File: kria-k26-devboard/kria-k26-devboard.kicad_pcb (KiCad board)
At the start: 8 copper layers, 121.5 x 89.8 mm, 225 parts, among them IC1 TPS2378DDA, IC2 USB5534B-5000JZX, J1 5-2337992-8, J2 USB4105-GF-A, J3 DC_SOCKET, J6 685119134923_, J7 WE_68715014022, M1 XILINX-KRIA-K26, P1 2199119-6, Q1 PJA3441, Q2 BSS138DW-7-F, U1 FT4232HPQ, U10 AP62301WU-7, U11 AP62301WU-7, U12 LTC4358CDE, U13 LTC4358CDE, U14 LTC4358CDE, U15 DP83867CRRGZR, U16 USB3310C-CP, U17 TPD4E05U06QDQARQ1, U18 TPD4E05U06QDQARQ1, U19 GSB3112311HR, U2 AP62301WU-7, U20 TPD4E05U06QDQARQ1, U21 TPD4E05U06QDQARQ1, U22 GSB3112311HR, U23 NVT4858HKZ, U3 MAX5984AETI+T, U4 AP62301WU-7, U5 AP62301WU-7, U6 AP62301WU-7, U7 AP62301WU-7, U8 RPX-4.0-R, U9 AP62301WU-7, Y1 ABM8G-25.000MHZ-18-D2Y-T

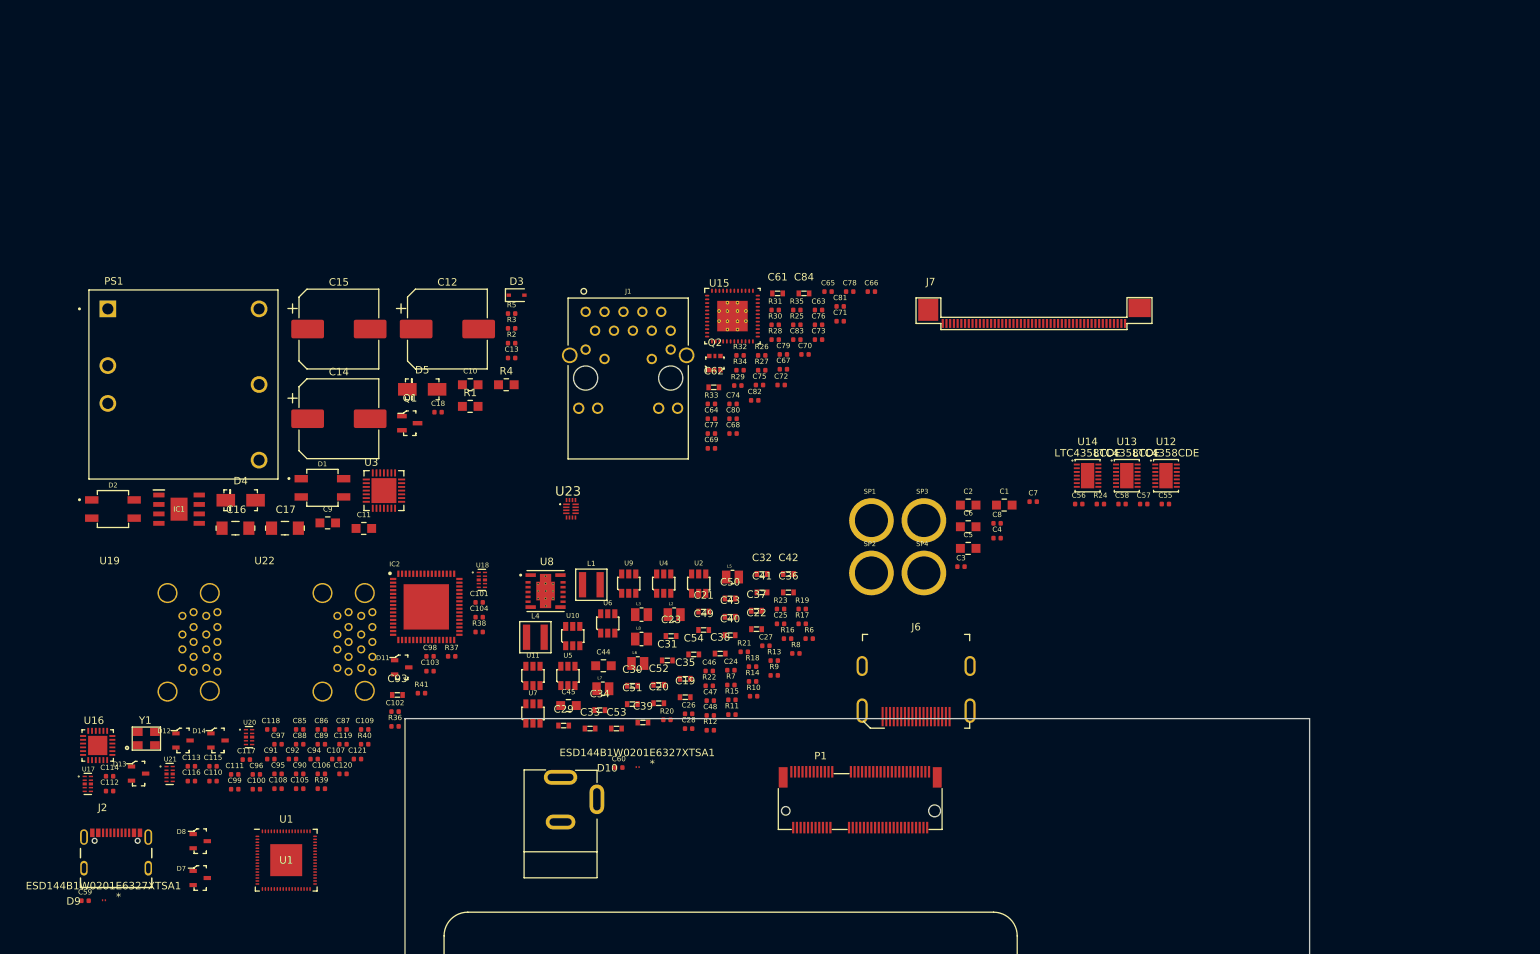
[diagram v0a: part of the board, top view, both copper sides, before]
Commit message: Finished reset logic, added crystal gen. to USB PHY, create power toggle for SD 3.0
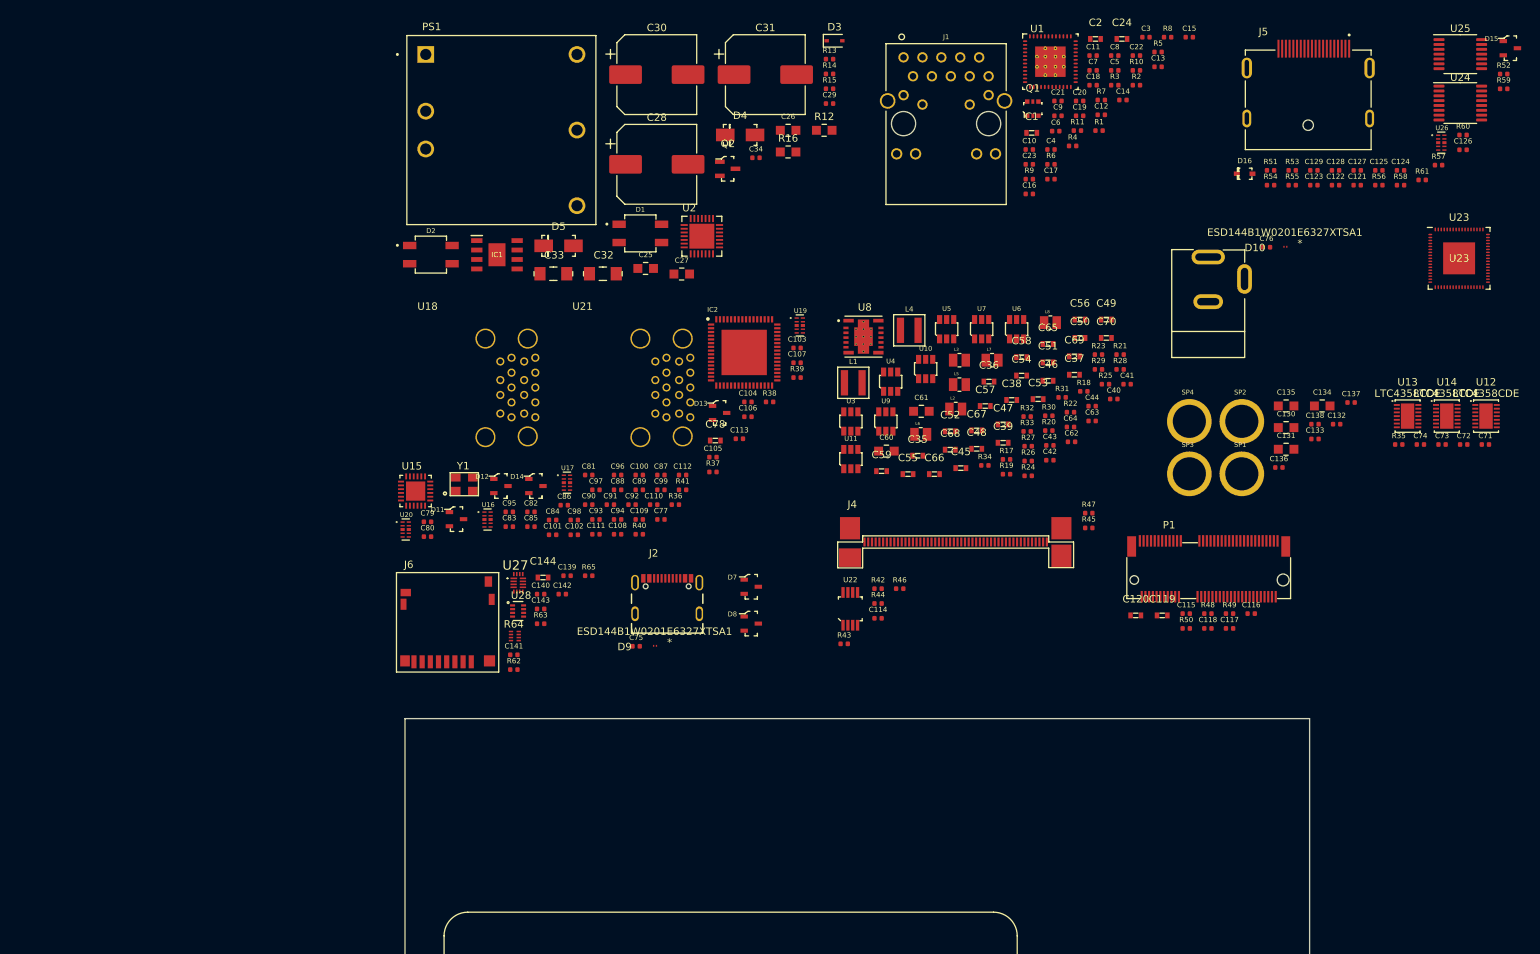
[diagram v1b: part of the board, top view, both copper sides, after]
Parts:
- removed J7: WE_68715014022, antmicro-footprints:WE_68715014022
- added C122: C_100n_0402, antmicro-footprints:0402-cap, F.Cu at (201.2, -24.5)
- added C123: C_100n_0402, antmicro-footprints:0402-cap, F.Cu at (198.3, -24.5)
- added C124: C_100n_0402, antmicro-footprints:0402-cap, F.Cu at (209.9, -26.5)
- added C125: C_100n_0402, antmicro-footprints:0402-cap, F.Cu at (207.0, -26.5)
- added C126: C_100n_0402, antmicro-footprints:0402-cap, F.Cu at (218.3, -29.3)
- added C127: C_100n_0402, antmicro-footprints:0402-cap, F.Cu at (204.1, -26.5)
- added C128: C_100n_0402, antmicro-footprints:0402-cap, F.Cu at (201.2, -26.5)
- added C129: C_100n_0402, antmicro-footprints:0402-cap, F.Cu at (198.3, -26.5)
- added C130: C_47u_0805, antmicro-footprints:0805-cap, F.Cu at (194.6, 8.06)
- added C131: C_47u_0805, antmicro-footprints:0805-cap, F.Cu at (194.6, 11.0)
- added C132: C_1u_0402, antmicro-footprints:0402-cap, F.Cu at (201.3, 7.61)
- added C133: C_100n_0402, antmicro-footprints:0402-cap, F.Cu at (198.4, 9.60)
- added C134: C_47u_0805, antmicro-footprints:0805-cap, F.Cu at (199.4, 5.16)
- added C135: C_47u_0805, antmicro-footprints:0805-cap, F.Cu at (194.6, 5.16)
- added C136: C_1u_0402, antmicro-footprints:0402-cap, F.Cu at (193.6, 13.4)
- added C137: C_100n_0402, antmicro-footprints:0402-cap, F.Cu at (203.3, 4.70)
- added C138: C_100n_0402, antmicro-footprints:0402-cap, F.Cu at (198.4, 7.61)
- added C139: C_100n_0402, antmicro-footprints:0402-cap, F.Cu at (98.0, 28.0)
- added C140: C_100n_0402, antmicro-footprints:0402-cap, F.Cu at (94.4, 30.4)
- added C141: C_100n_0402, antmicro-footprints:0402-cap, F.Cu at (90.8, 38.6)
- added C142: C_100n_0402, antmicro-footprints:0402-cap, F.Cu at (97.3, 30.4)
- added C143: C_100n_0402, antmicro-footprints:0402-cap, F.Cu at (94.4, 32.4)
- added C144: C_10u_0603, antmicro-footprints:0603-cap, F.Cu at (94.7, 28.2)
- added D15: PESD2USB5UV-TR, antmicro-footprints:SOT-23s, F.Cu at (224.7, -42.9)
- added D16: PMEG3010CEJ, antmicro-footprints:SOD-323F, F.Cu at (189.0, -26.0)
- added J4: WE_68715014522, antmicro-footprints:WE_68715014522, F.Cu at (150.2, 22.8)
- added J5: 47272-0001, antmicro-footprints:MOLEX_47272-0001, F.Cu at (197.5, -29.3)
- added R42: R_2k2_0402, antmicro-footprints:0402-res, F.Cu at (139.7, 29.7)
- added R43: R_2k2_0402, antmicro-footprints:0402-res, F.Cu at (135.2, 37.1)
- added R44: R_2k2_0402, antmicro-footprints:0402-res, F.Cu at (139.7, 31.7)
- added R45: R_2k2_0402, antmicro-footprints:0402-res, F.Cu at (168.0, 21.5)
- added R46: R_2k2_0402, antmicro-footprints:0402-res, F.Cu at (142.6, 29.7)
- added R47: R_2k2_0402, antmicro-footprints:0402-res, F.Cu at (168.0, 19.6)
- added R48: R_10k_0402, antmicro-footprints:0402-res, F.Cu at (184.0, 33.1)
- added R49: R_10k_0402, antmicro-footprints:0402-res, F.Cu at (187.0, 33.1)
- added R50: R_10k_0402, antmicro-footprints:0402-res, F.Cu at (181.1, 35.0)
- added R51: R_49R9_0402, antmicro-footprints:0402-res, F.Cu at (192.5, -26.5)
- added R52: R_49R9_0402, antmicro-footprints:0402-res, F.Cu at (223.8, -39.4)
- added R53: R_2k49_0402, antmicro-footprints:0402-res, F.Cu at (195.4, -26.5)
- added R54: R_1k5_0402, antmicro-footprints:0402-res, F.Cu at (192.5, -24.5)
- added R55: R_100k_0402, antmicro-footprints:0402-res, F.Cu at (195.4, -24.5)
- added R56: R_100k_0402, antmicro-footprints:0402-res, F.Cu at (207.0, -24.5)
- added R57: R_1M0_0402, antmicro-footprints:0402-res, F.Cu at (215.0, -27.2)
- added R58: R_0R_0402, antmicro-footprints:0402-res, F.Cu at (209.9, -24.5)
- added R59: R_0R_0402, antmicro-footprints:0402-res, F.Cu at (223.8, -37.4)
- added R60: R_100k_0402, antmicro-footprints:0402-res, F.Cu at (218.3, -31.2)
- added R61: R_1M0_0402, antmicro-footprints:0402-res, F.Cu at (212.8, -25.2)
- added R62: R_33R_0402, antmicro-footprints:0402-res, F.Cu at (90.8, 40.6)
- added R63: R_33R_0402, antmicro-footprints:0402-res, F.Cu at (94.4, 34.4)
- added R64: 4x33R_0201_array, antmicro-footprints:EXB18V, F.Cu at (90.9, 36.1)
- added R65: R_10k_0402, antmicro-footprints:0402-res, F.Cu at (100.9, 28.0)
- added U24: SN74AVC4T245PWR, Package_SO:TSSOP-16_4.4x5mm_P0.65mm, F.Cu at (218.0, -35.5)
- added U25: FIN1019MTC, antmicro-footprints:TSSOP-14_4.4x5mm_P0.65mm, F.Cu at (218.0, -42.1)
- added U26: TPD4E05U06QDQARQ1, antmicro-footprints:TPD4E05U06QDQARQ1, F.Cu at (215.4, -30.2)
- added U27: NVT4858HKZ, antmicro-footprints:SOT1161-2, F.Cu at (91.4, 28.9)
- added U28: TPS2116DRLR, antmicro-footprints:Texas_DRL0008A, F.Cu at (91.4, 32.7)
- C1, C2: value C_47u_0805 -> C_10u_0603; footprint antmicro-footprints:0805-cap -> antmicro-footprints:0603-cap
- C10, C11: value C_100n_0805_100V -> C_100n_0402; footprint antmicro-footprints:0805-cap -> antmicro-footprints:0402-cap
- C111, C112: value C_100n_0402 -> C_4u7_0402
- C114, C117: value C_18p_0402 -> C_100n_0402
- C119, C120, C24, C78: value C_100n_0402 -> C_10u_0603; footprint antmicro-footprints:0402-cap -> antmicro-footprints:0603-cap
- C12, C14, C15: value C_47u_ELEC_100V -> C_100n_0402; footprint antmicro-footprints:CP_Elec_10x10.5 -> antmicro-footprints:0402-cap
- C13: value C_1n0_0402 -> C_100n_0402
- C16, C17: value C_47u_16V_1206 -> C_100n_0402; footprint antmicro-footprints:1206-cap -> antmicro-footprints:0402-cap
- C18: value C_100n_0402_16V -> C_100n_0402
- C19, C20, C21, C22: value C_10u_25V_0603 -> C_1u_0402; footprint antmicro-footprints:0603-cap -> antmicro-footprints:0402-cap
- C23: value C_10u_25V_0603 -> C_10n_0402; footprint antmicro-footprints:0603-cap -> antmicro-footprints:0402-cap
- C25, C26, C27: value C_100n_0402 -> C_100n_0805_100V; footprint antmicro-footprints:0402-cap -> antmicro-footprints:0805-cap
- C28: value C_100n_0402 -> C_47u_ELEC_100V; footprint antmicro-footprints:0402-cap -> antmicro-footprints:CP_Elec_10x10.5
- C29: value C_10u_25V_0603 -> C_1n0_0402; footprint antmicro-footprints:0603-cap -> antmicro-footprints:0402-cap
- C3: value C_1u_0402 -> C_10n_0402
- C30, C31: value C_22u_0603 -> C_47u_ELEC_100V; footprint antmicro-footprints:0603-cap -> antmicro-footprints:CP_Elec_10x10.5
- C32, C33: value C_22u_0603 -> C_47u_16V_1206; footprint antmicro-footprints:0603-cap -> antmicro-footprints:1206-cap
- C34: value C_22u_0603 -> C_100n_0402_16V; footprint antmicro-footprints:0603-cap -> antmicro-footprints:0402-cap
- C35, C36, C37, C38, C39: value C_22u_0603 -> C_10u_25V_0603
- C4: value C_100n_0402 -> C_10n_0402
- C40, C41, C42, C43: value C_10u_25V_0603 -> C_100n_0402; footprint antmicro-footprints:0603-cap -> antmicro-footprints:0402-cap
- C44: value C_47u_0805 -> C_100n_0402; footprint antmicro-footprints:0805-cap -> antmicro-footprints:0402-cap
- C45: value C_47u_0805 -> C_10u_25V_0603; footprint antmicro-footprints:0805-cap -> antmicro-footprints:0603-cap
- C46, C47, C48, C55, C70: value C_100n_0402 -> C_22u_0603; footprint antmicro-footprints:0402-cap -> antmicro-footprints:0603-cap
- C5, C6: value C_47u_0805 -> C_1u_0402; footprint antmicro-footprints:0805-cap -> antmicro-footprints:0402-cap
- C56, C57, C58: value C_100n_0402 -> C_10u_25V_0603; footprint antmicro-footprints:0402-cap -> antmicro-footprints:0603-cap
- C59: value C_100n_0402_50V -> C_10u_25V_0603; footprint antmicro-footprints:0402-cap -> antmicro-footprints:0603-cap
- C60: value C_100n_0402_50V -> C_47u_0805; footprint antmicro-footprints:0402-cap -> antmicro-footprints:0805-cap
- C61: value C_10u_0603 -> C_47u_0805; footprint antmicro-footprints:0603-cap -> antmicro-footprints:0805-cap
- C62, C84, C93: value C_10u_0603 -> C_100n_0402; footprint antmicro-footprints:0603-cap -> antmicro-footprints:0402-cap
- C63, C64, C83: value C_10n_0402 -> C_100n_0402
- C65, C66, C67, C68, C69: value C_1u_0402 -> C_22u_0603; footprint antmicro-footprints:0402-cap -> antmicro-footprints:0603-cap
- C75, C76: value C_100n_0402 -> C_100n_0402_50V
- C77, C8: value C_100n_0402 -> C_1u_0402
- C79, C80, C81, C82: value C_1u_0402 -> C_100n_0402
- C87: value C_100n_0402 -> C_18p_0402
- C88: value C_2u2_0402 -> C_100n_0402
- C9: value C_100n_0805_100V -> C_1u_0402; footprint antmicro-footprints:0805-cap -> antmicro-footprints:0402-cap
- C92: value C_1u_0402 -> C_18p_0402
- C98: value C_4u7_0402 -> C_2u2_0402
- C99: value C_4u7_0402 -> C_100n_0402
- J6: value 685119134923_ -> 1140084168; footprint antmicro-footprints:HDMI_A_Female_685119134923 -> antmicro-footprints:MicroSD_1140084168
- Q1: value PJA3441 -> BSS138DW-7-F; footprint antmicro-footprints:SOT-23-3 -> antmicro-footprints:SOT-363
- Q2: value BSS138DW-7-F -> PJA3441; footprint antmicro-footprints:SOT-363 -> antmicro-footprints:SOT-23-3
- R1: value R_2M2_0805 -> R_5k76_0402; footprint antmicro-footprints:0805-res -> antmicro-footprints:0402-res
- R10: value R_12k4_0402 -> R_330R_0402
- R11: value R_10k_0402 -> R_330R_0402
- R12: value R_4k99_0402 -> R_2M2_0805; footprint antmicro-footprints:0402-res -> antmicro-footprints:0805-res
- R13: value R_10k_0402 -> R_24k9_0402
- R14: value R_2k49_0402 -> R_63R4_0402
- R15: value R_10k_0402 -> R_0R_0402
- R16: value R_10k_0402 -> R_100k_0805; footprint antmicro-footprints:0402-res -> antmicro-footprints:0805-res
- R17: value R_2k49_0402 -> R_31k6_0402
- R18: value R_31k6_0402 -> R_10k_0402
- R19: value R_10k_0402 -> R_21k5_0402
- R2: value R_24k9_0402 -> R_2k49_0402
- R20: value R_12k4_0402 -> R_10k_0402
- R21: value R_10k_0402 -> R_12k4_0402
- R22: value R_4k99_0402 -> R_10k_0402
- R23: value R_10k_0402 -> R_4k99_0402
- R24: value R_100R_0402 -> R_10k_0402
- R25: value R_5k76_0402 -> R_2k49_0402
- R26: value R_2k49_0402 -> R_10k_0402
- R28: value R_2k2_0402 -> R_2k49_0402
- R29: value R_11k_0402 -> R_31k6_0402
- R3: value R_63R4_0402 -> R_10k_0402
- R30, R32: value R_4k7_0402 -> R_10k_0402
- R31: value R_4k7_0402 -> R_12k4_0402
- R33: value R_2k2_0402 -> R_4k99_0402
- R34: value R_330R_0402 -> R_10k_0402
- R35: value R_330R_0402 -> R_100R_0402
- R36: value R_10k_0402 -> R_12k_0402
- R37: value R_8k06_0402 -> R_10k_0402
- R38: value R_12k_0402 -> R_8k06_0402
- R4: value R_100k_0805 -> R_2k2_0402; footprint antmicro-footprints:0805-res -> antmicro-footprints:0402-res
- R5: value R_0R_0402 -> R_11k_0402
- R6: value R_31k6_0402 -> R_4k7_0402
- R7: value R_10k_0402 -> R_4k7_0402
- R8: value R_21k5_0402 -> R_4k7_0402
- R9: value R_10k_0402 -> R_2k2_0402
- U1: value FT4232HPQ -> DP83867CRRGZR; footprint antmicro-footprints:QFN-68_EP_8x8_Pitch0.4mm -> antmicro-footprints:Texas-VQFN-48
- U15: value DP83867CRRGZR -> USB3310C-CP; footprint antmicro-footprints:Texas-VQFN-48 -> antmicro-footprints:Microchip_QFN24_4X4
- U16: value USB3310C-CP -> TPD4E05U06QDQARQ1; footprint antmicro-footprints:Microchip_QFN24_4X4 -> antmicro-footprints:TPD4E05U06QDQARQ1
- U18, U21: value TPD4E05U06QDQARQ1 -> GSB3112311HR; footprint antmicro-footprints:TPD4E05U06QDQARQ1 -> antmicro-footprints:GSB3112311HR
- U19: value GSB3112311HR -> TPD4E05U06QDQARQ1; footprint antmicro-footprints:GSB3112311HR -> antmicro-footprints:TPD4E05U06QDQARQ1
- U2: value AP62301WU-7 -> MAX5984AETI+T; footprint antmicro-footprints:TSOT23-6 -> antmicro-footprints:Maxim_MAX5984_TQFN-EP-28
- U22: value GSB3112311HR -> PI4MSD5V9540BUEX; footprint antmicro-footprints:GSB3112311HR -> antmicro-footprints:MSOP-8_W3mm_PITCH0.65mm
- U23: value NVT4858HKZ -> FT4232HPQ; footprint antmicro-footprints:SOT1161-2 -> antmicro-footprints:QFN-68_EP_8x8_Pitch0.4mm
- U3: value MAX5984AETI+T -> AP62301WU-7; footprint antmicro-footprints:Maxim_MAX5984_TQFN-EP-28 -> antmicro-footprints:TSOT23-6
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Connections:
- net /Xilinx K26 SOM/GTR_REFCLK3_C2M_N renamed /Clock distribution/GTR_REFCLK3_C2M_N
- net /Xilinx K26 SOM/GTR_REFCLK3_C2M_P renamed /Clock distribution/GTR_REFCLK3_C2M_P
- net Net-(P1-Pad3) renamed /PCIE M2 key E /M2_USB_P
- net Net-(P1-Pad47) renamed /Clock distribution/GTR_REFCLK3_P
- net Net-(P1-Pad49) renamed /Clock distribution/GTR_REFCLK3_N
- net Net-(P1-Pad5) renamed /PCIE M2 key E /M2_USB_N
- C1 pad 1: SOM_5V0 -> PS_1V8
- C10 pad 1: /Power Supply/PoE/VDD_POE_IN -> PS_1V8
- C10 pad 2: /Power Supply/PoE/VSS_POE_IN -> GND
- C100 pad 2: /USB/USB3_TX_N -> /USB/USB1_TX_N
- C101 pad 2: /USB/USB3_TX_P -> /USB/USB1_TX_P
- C102 pad 2: /USB/USB4_TX_N -> /USB/USB2_TX_N
- C103 pad 2: /USB/USB4_TX_P -> /USB/USB2_TX_P
- C105 pad 1: /USB/USB1_VBUS -> /USB/USB2_VBUS
- C106 pad 1: PS_3V3 -> Net-(C106-Pad1)
- C106 pad 2: Net-(C106-Pad2) -> GND
- C107 pad 1: PS_1V2 -> Net-(C107-Pad1)
- C107 pad 2: Net-(C107-Pad2) -> /USB/USB3_TX_N
- C108 pad 1: PS_3V3 -> Net-(C108-Pad1)
- C108 pad 2: Net-(C106-Pad2) -> /USB/USB3_TX_P
- C109 pad 1: PS_1V2 -> Net-(C109-Pad1)
- C109 pad 2: Net-(C107-Pad2) -> /USB/USB4_TX_N
- C11 pad 1: /Power Supply/PoE/VDD_POE_OUT -> PS_1V8
- C11 pad 2: /Power Supply/PoE/VSS_POE_IN -> GND
- C110 pad 1: PS_3V3 -> Net-(C110-Pad1)
- C110 pad 2: Net-(C106-Pad2) -> /USB/USB4_TX_P
- C111 pad 1: PS_1V2 -> /USB/USB3_VBUS
- C111 pad 2: Net-(C107-Pad2) -> GND
- C112 pad 1: PS_1V2 -> /USB/USB4_VBUS
- C112 pad 2: Net-(C107-Pad2) -> GND
- C113 pad 1: PS_3V3 -> Net-(C113-Pad1)
- C113 pad 2: Net-(C106-Pad2) -> GND
- C114 pad 1: /USB/XIN -> PL_3V3
- C115 pad 1: PS_1V2 -> /PCIE M2 key E /GTR_DP3_M2C_C_P
- C115 pad 2: Net-(C107-Pad2) -> /PCIE M2 key E /GTR_DP3_M2C_P
- C116 pad 1: PS_1V2 -> /PCIE M2 key E /GTR_DP3_M2C_C_N
- C116 pad 2: Net-(C107-Pad2) -> /PCIE M2 key E /GTR_DP3_M2C_N
- C117 pad 1: /USB/XOUT -> PS_3V3
- C118 pad 1: PS_1V2 -> PS_3V3
- C118 pad 2: Net-(C107-Pad2) -> GND
- C119 pad 1: PS_1V2 -> PS_3V3
- C119 pad 2: Net-(C107-Pad2) -> GND
- C12 pad 1: /Power Supply/PoE/VDD_POE_OUT -> PS_1V8
- C12 pad 2: /Power Supply/PoE/VSS_POE_IN -> GND
- C120 pad 1: Net-(C120-Pad1) -> PS_3V3
- C121 pad 1: Net-(C121-Pad1) -> GND
- C121 pad 2: GND -> PS_1V8
- C13 pad 1: Net-(C13-Pad1) -> PS_2V5
- C13 pad 2: /Power Supply/PoE/VSS_POE_IN -> GND
- C14 pad 1: /Power Supply/PoE/VDD_POE_IN -> PS_2V5
- C14 pad 2: GNDD -> GND
- C15 pad 1: /Power Supply/PoE/VDD_POE_IN -> PS_1V0
- C15 pad 2: GNDD -> GND
- C16 pad 1: /Power Supply/PoE/POE_12V -> PS_1V0
- C17 pad 1: /Power Supply/PoE/POE_12V -> PS_1V0
- C18 pad 1: /Power Supply/PoE/POE_12V -> PS_1V0
- C19 pad 1: /Power Supply/DC/DC conventers/DC_MAIN_BUS -> PS_1V0
- C2 pad 1: SOM_5V0 -> PS_2V5
- C20 pad 1: /Power Supply/DC/DC conventers/DC_MAIN_BUS -> PS_1V0
- C21 pad 1: /Power Supply/DC/DC conventers/DC_MAIN_BUS -> PS_1V0
- C22 pad 1: /Power Supply/DC/DC conventers/DC_MAIN_BUS -> PS_1V0
- C23 pad 1: /Power Supply/DC/DC conventers/DC_MAIN_BUS -> PS_1V0
- C24 pad 1: Net-(C24-Pad1) -> PS_1V0
- C24 pad 2: Net-(C24-Pad2) -> GND
- C25 pad 1: Net-(C25-Pad1) -> /Power Supply/PoE/VDD_POE_OUT
- C25 pad 2: Net-(C25-Pad2) -> /Power Supply/PoE/VSS_POE_OUT
- C26 pad 1: Net-(C26-Pad1) -> /Power Supply/PoE/VDD_POE_IN
- C26 pad 2: Net-(C26-Pad2) -> /Power Supply/PoE/VSS_POE_IN
- C27 pad 1: Net-(C27-Pad1) -> /Power Supply/PoE/VDD_POE_OUT
- C27 pad 2: Net-(C27-Pad2) -> /Power Supply/PoE/VSS_POE_IN
- C28 pad 1: Net-(C28-Pad1) -> /Power Supply/PoE/VDD_POE_OUT
- C28 pad 2: Net-(C28-Pad2) -> /Power Supply/PoE/VSS_POE_IN
- C29 pad 1: /Power Supply/DC/DC conventers/DC_MAIN_BUS -> Net-(C29-Pad1)
- C29 pad 2: Net-(C29-Pad2) -> /Power Supply/PoE/VSS_POE_IN
- C3 pad 1: SOM_5V0 -> PS_1V8
- C30 pad 1: GND -> /Power Supply/PoE/VDD_POE_IN
- C30 pad 2: PS_3V3 -> GNDD
- C31 pad 1: GND -> /Power Supply/PoE/VDD_POE_IN
- C31 pad 2: PS_2V5 -> GNDD
- C32 pad 1: GND -> /Power Supply/PoE/POE_12V
- C32 pad 2: PS_1V8 -> GND
- C33 pad 1: GND -> /Power Supply/PoE/POE_12V
- C33 pad 2: PS_1V2 -> GND
- C34 pad 1: GND -> /Power Supply/PoE/POE_12V
- C34 pad 2: PS_1V0 -> GND
- C35 pad 1: GND -> /Power Supply/DC/DC conventers/DC_MAIN_BUS
- C35 pad 2: PS_3V3 -> GND
- C36 pad 1: GND -> /Power Supply/DC/DC conventers/DC_MAIN_BUS
- C36 pad 2: PS_2V5 -> GND
- C37 pad 1: GND -> /Power Supply/DC/DC conventers/DC_MAIN_BUS
- C37 pad 2: PS_1V8 -> GND
- C38 pad 1: GND -> /Power Supply/DC/DC conventers/DC_MAIN_BUS
- C38 pad 2: PS_1V2 -> GND
- C39 pad 1: GND -> /Power Supply/DC/DC conventers/DC_MAIN_BUS
- C39 pad 2: PS_1V0 -> GND
- C4 pad 1: SOM_5V0 -> PS_2V5
- C40 pad 1: /Power Supply/DC/DC conventers/DC_MAIN_BUS -> Net-(C40-Pad1)
- C40 pad 2: Net-(C29-Pad2) -> Net-(C40-Pad2)
- C41 pad 1: /Power Supply/DC/DC conventers/DC_MAIN_BUS -> Net-(C41-Pad1)
- C41 pad 2: GND -> Net-(C41-Pad2)
- C42 pad 1: /Power Supply/DC/DC conventers/DC_MAIN_BUS -> Net-(C42-Pad1)
- C42 pad 2: GND -> Net-(C42-Pad2)
- C43 pad 1: /Power Supply/DC/DC conventers/DC_MAIN_BUS -> Net-(C43-Pad1)
- C43 pad 2: GND -> Net-(C43-Pad2)
- C44 pad 1: SOM_5V -> Net-(C44-Pad1)
- C45 pad 1: SOM_5V -> /Power Supply/DC/DC conventers/DC_MAIN_BUS
- C45 pad 2: Net-(C44-Pad2) -> Net-(C45-Pad2)
- C46 pad 1: Net-(C46-Pad1) -> GND
- C46 pad 2: Net-(C46-Pad2) -> PS_3V3
- C47 pad 1: Net-(C47-Pad1) -> GND
- C47 pad 2: Net-(C47-Pad2) -> PS_2V5
- C48 pad 1: Net-(C48-Pad1) -> GND
- C48 pad 2: Net-(C48-Pad2) -> PS_1V8
- C49 pad 2: PL_3V3 -> PS_1V2
- C5 pad 1: SOM_5V0 -> PS_1V8
- C50 pad 2: PL_1V8 -> PS_1V0
- C51 pad 2: PL_1V2 -> PS_3V3
- C52 pad 2: PL_3V3 -> PS_2V5
- C53 pad 2: PL_1V8 -> PS_1V8
- C54 pad 2: PL_1V2 -> PS_1V2
- C55 pad 1: Net-(C55-Pad1) -> GND
- C55 pad 2: Net-(C55-Pad2) -> PS_1V0
- C56 pad 2: GND -> Net-(C45-Pad2)
- C58 pad 2: Net-(C55-Pad2) -> GND
- C59 pad 1: VBUS -> /Power Supply/DC/DC conventers/DC_MAIN_BUS
- C6 pad 1: SOM_5V0 -> PS_1V8
- C60 pad 1: /Power Supply/DC Input/DC_IN -> SOM_5V
- C60 pad 2: GND -> Net-(C60-Pad2)
- C61 pad 1: PS_1V8 -> SOM_5V
- C61 pad 2: GND -> Net-(C60-Pad2)
- C62 pad 1: PS_2V5 -> Net-(C62-Pad1)
- C62 pad 2: GND -> Net-(C62-Pad2)
- C63 pad 1: PS_1V8 -> Net-(C63-Pad1)
- C63 pad 2: GND -> Net-(C63-Pad2)
- C64 pad 1: PS_2V5 -> Net-(C64-Pad1)
- C64 pad 2: GND -> Net-(C64-Pad2)
- C65 pad 1: PS_1V8 -> GND
- C65 pad 2: GND -> PL_3V3
- C66 pad 1: PS_1V8 -> GND
- C66 pad 2: GND -> PL_1V8
- C67 pad 1: PS_1V8 -> GND
- C67 pad 2: GND -> PL_1V2
- C68 pad 1: PS_2V5 -> GND
- C68 pad 2: GND -> PL_3V3
- C69 pad 1: PS_2V5 -> GND
- C69 pad 2: GND -> PL_1V8
- C7 pad 1: SOM_5V0 -> PS_1V8
- C70 pad 1: PS_1V8 -> GND
- C70 pad 2: GND -> PL_1V2
- C71 pad 1: PS_1V8 -> Net-(C71-Pad1)
- C71 pad 2: GND -> Net-(C71-Pad2)
- C72 pad 1: PS_1V8 -> /Power Supply/DC/DC conventers/DC_MAIN_BUS
- C73 pad 1: PS_2V5 -> /Power Supply/DC/DC conventers/DC_MAIN_BUS
- C74 pad 1: PS_2V5 -> /Power Supply/DC/DC conventers/DC_MAIN_BUS
- C74 pad 2: GND -> Net-(C71-Pad2)
- C75 pad 1: PS_1V0 -> VBUS
- C76 pad 1: PS_1V0 -> /Power Supply/DC Input/DC_IN
- C77 pad 1: PS_1V0 -> PS_3V3
- C77 pad 2: GND -> Net-(C77-Pad2)
- C78 pad 1: PS_1V0 -> PS_1V2
- C78 pad 2: GND -> Net-(C78-Pad2)
- C79 pad 1: PS_1V0 -> PS_3V3
- C79 pad 2: GND -> Net-(C77-Pad2)
- C8 pad 1: SOM_5V0 -> PS_2V5
- C80 pad 1: PS_1V0 -> PS_1V2
- C80 pad 2: GND -> Net-(C78-Pad2)
- C81 pad 1: PS_1V0 -> PS_3V3
- C81 pad 2: GND -> Net-(C77-Pad2)
- C82 pad 1: PS_1V0 -> PS_1V2
- C82 pad 2: GND -> Net-(C78-Pad2)
- C83 pad 1: PS_1V0 -> PS_3V3
- C83 pad 2: GND -> Net-(C77-Pad2)
- C84 pad 1: PS_1V0 -> PS_1V2
- C84 pad 2: GND -> Net-(C78-Pad2)
- C85 pad 1: PS_1V8 -> PS_1V2
- C85 pad 2: GND -> Net-(C78-Pad2)
- C86 pad 1: PS_1V8 -> PS_3V3
- C86 pad 2: GND -> Net-(C77-Pad2)
- C87 pad 1: PS_1V8 -> /USB/XIN
- C88 pad 1: Net-(C88-Pad1) -> PS_1V2
- C88 pad 2: GND -> Net-(C78-Pad2)
- C89 pad 1: SOM_5V -> /USB/GTR_DP2_C2M_C_P
- C89 pad 2: GND -> /USB/GTR_DP2_C2M_P
- C9 pad 1: /Power Supply/PoE/VDD_POE_OUT -> PS_2V5
- C9 pad 2: /Power Supply/PoE/VSS_POE_OUT -> GND
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
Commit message: Progress on Debug sheet
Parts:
- added C145: C_100n_0402, antmicro-footprints:0402-cap, F.Cu at (103.3, -34.5)
- added C146: C_470n_0402, antmicro-footprints:0402-cap, F.Cu at (180.1, -30.8)
- added C147: C_470n_0402, antmicro-footprints:0402-cap, F.Cu at (183.2, -33.9)
- added C148: C_100n_0402, antmicro-footprints:0402-cap, F.Cu at (169.2, -45.6)
- added C149: C_100n_0402, antmicro-footprints:0402-cap, F.Cu at (183.4, -53.4)
- added C150: C_47n_0402, antmicro-footprints:0402-cap, F.Cu at (173.9, -47.5)
- added C151: C_47n_0402, antmicro-footprints:0402-cap, F.Cu at (169.2, -43.6)
- added C152: C_100n_0402, antmicro-footprints:0402-cap, F.Cu at (182.8, -55.4)
- added C153: C_100n_0402, antmicro-footprints:0402-cap, F.Cu at (180.5, -52.8)
- added C154: C_100n_0402, antmicro-footprints:0402-cap, F.Cu at (185.7, -57.4)
- added C155: C_100n_0402, antmicro-footprints:0402-cap, F.Cu at (172.1, -45.5)
- added C156: C_100n_0402, antmicro-footprints:0402-cap, F.Cu at (176.8, -47.5)
- added Q3: BSS123, antmicro-footprints:SOT-23-3, F.Cu at (176.2, -36.3)
- added Q4: AO3401A, antmicro-footprints:SOT-23-3, F.Cu at (176.2, -31.3)
- added R66: R_1k_0402, antmicro-footprints:0402-res, F.Cu at (184.8, -28.8)
- added R67: R_10k_0402, antmicro-footprints:0402-res, F.Cu at (180.5, -50.8)
- added R68: R_10k_0402, antmicro-footprints:0402-res, F.Cu at (185.7, -55.4)
- added R69: R_10k_0402, antmicro-footprints:0402-res, F.Cu at (172.1, -43.5)
- added R70: R_10k_0402, antmicro-footprints:0402-res, F.Cu at (175.0, -45.5)
- added R71: R_10k_0402, antmicro-footprints:0402-res, F.Cu at (182.8, -57.4)
- added S1: KMR2, antmicro-footprints:SW_SPST_4.2x2.8, F.Cu at (177.8, -56.1)
- added U29: SN74AVC4T245PWR, Package_SO:TSSOP-16_4.4x5mm_P0.65mm, F.Cu at (169.9, -55.1)
- added U30: SN74AVC4T245PWR, Package_SO:TSSOP-16_4.4x5mm_P0.65mm, F.Cu at (163.4, -46.4)
- added U31: TPS3840PH30DBVR, antmicro-footprints:SOT-23-5, F.Cu at (176.7, -51.1)
- added U32: TPS3840PH30DBVR, antmicro-footprints:SOT-23-5, F.Cu at (170.1, -49.2)
- added U33: 74LV07ATPWJ, antmicro-footprints:TSSOP-14_W4.4mm, F.Cu at (162.3, -54.0)
- added XTAL1: SIT1602BC-13-18E-24.000000G, antmicro-footprints:SiTIME_SMD-6-1EP, F.Cu at (58.5, -24.2)
- moved D10 123.9 mm to (70.6, -12.5)
- moved C76 123.9 mm to (68.1, -12.5)
- moved J3 123.9 mm to (60.3, 2.53)
- moved C141 118.3 mm to (185.9, -31.9)
- moved R62 114.5 mm to (181.9, -28.8)
- moved R64 113.1 mm to (180.2, -33.3)
- moved C144 110.8 mm to (184.0, -37.5)
- moved U27 110.8 mm to (180.7, -36.8)
- moved J6 107.1 mm to (166.5, -31.5)
- moved C142 105.3 mm to (183.0, -30.8)
- moved C140 104.5 mm to (181.9, -26.8)
- moved R63 104.5 mm to (181.2, -23.9)
- moved U28 103.5 mm to (175.9, -27.0)
- moved C143 98.8 mm to (175.4, -24.2)
- moved C139 95.6 mm to (178.3, -23.9)
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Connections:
- IC2 pad 50: Net-(IC2-Pad50) -> /Reset logic/USB_HUB_RESET
- J4 pad 32: Net-(J4-Pad32) -> /Camera interfaces/CAM0_PWDN
- J4 pad 33: Net-(J4-Pad33) -> /Camera interfaces/CAM0_RST
- J4 pad 34: Net-(J4-Pad34) -> /Camera interfaces/CAM1_PWDN
- J_SOM240_1 pad A15: /Xilinx K26 SOM/HDA09 -> /Reset logic/HDA09
- J_SOM240_1 pad A36: /Xilinx K26 SOM/MIO43 -> /Reset logic/MIO43
- J_SOM240_1 pad B13: /Xilinx K26 SOM/VCCO_HDA -> PL_3V3
- J_SOM240_1 pad B14: /Xilinx K26 SOM/VCCO_HDA -> PL_3V3
- J_SOM240_1 pad B17: /Xilinx K26 SOM/HDA04 -> /Reset logic/HDA04
- J_SOM240_1 pad B32: /Xilinx K26 SOM/MIO38 -> /Reset logic/MIO38
- J_SOM240_1 pad D01: PL_3V3 -> PL_1V2
- J_SOM240_1 pad D02: PL_3V3 -> PL_1V2
- J_SOM240_1 pad D18: /Xilinx K26 SOM/HDA02 -> /Reset logic/HDA02
- J_SOM240_1 pad D32: /Xilinx K26 SOM/MIO44 -> /Reset logic/MIO44
- R3 pad 1: PS_1V8 -> PS_3V3
- R3 pad 2: /Ethernet/ETH_RESET -> Net-(C146-Pad2)
- U15 pad 14: Net-(U15-Pad14) -> PS_1V8
- U15 pad 15: Net-(U15-Pad14) -> PS_1V8
- U15 pad 22: Net-(U15-Pad22) -> /Reset logic/USB_PHY_RESET

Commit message: Added second ETH interface, connect POE PSE
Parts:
- added C157: C_100n_0402, antmicro-footprints:0402-cap, F.Cu at (167.7, -73.5)
- added C158: C_10u_25V_0603, antmicro-footprints:0603-cap, F.Cu at (163.4, -77.7)
- added C159: C_100n_0402, antmicro-footprints:0402-cap, F.Cu at (169.8, -79.6)
- added C160: C_100n_0402, antmicro-footprints:0402-cap, F.Cu at (165.3, -71.5)
- added C161: C_100n_0402, antmicro-footprints:0402-cap, F.Cu at (157.7, -63.4)
- added C162: C_100n_0402, antmicro-footprints:0402-cap, F.Cu at (171.6, -75.6)
- added C163: C_100n_0402, antmicro-footprints:0402-cap, F.Cu at (165.3, -69.5)
- added C164: C_100n_0402, antmicro-footprints:0402-cap, F.Cu at (162.4, -66.3)
- added C165: C_100n_0402, antmicro-footprints:0402-cap, F.Cu at (157.7, -61.4)
- added C166: C_100n_0402, antmicro-footprints:0402-cap, F.Cu at (168.2, -71.5)
- added C167: C_100n_0402, antmicro-footprints:0402-cap, F.Cu at (162.4, -68.2)
- added C168: C_100n_0402, antmicro-footprints:0402-cap, F.Cu at (160.6, -64.3)
- added C169: C_4u7_0402, antmicro-footprints:0402-cap, F.Cu at (165.3, -67.5)
- added C170: C_100n_0402, antmicro-footprints:0402-cap, F.Cu at (170.5, -82.0)
- added C171: C_100n_0402, antmicro-footprints:0402-cap, F.Cu at (168.2, -69.5)
- added C172: C_100n_0402, antmicro-footprints:0402-cap, F.Cu at (171.1, -71.6)
- added C173: C_100n_0402, antmicro-footprints:0402-cap, F.Cu at (154.8, -60.1)
- added C174: C_33n_0402, antmicro-footprints:0402-cap, F.Cu at (134.3, -59.9)
- added C175: C_10u_0603, antmicro-footprints:0603-cap, F.Cu at (150.5, -70.2)
- added C176: C_18p_0402, antmicro-footprints:0402-cap, F.Cu at (150.8, -68.0)
- added C177: C_4u7_0402, antmicro-footprints:0402-cap, F.Cu at (153.7, -68.0)
- added C178: C_18p_0402, antmicro-footprints:0402-cap, F.Cu at (170.6, -73.6)
- added C179: C_100n_0402, antmicro-footprints:0402-cap, F.Cu at (169.5, -77.6)
- added C180: C_100n_0402, antmicro-footprints:0402-cap, F.Cu at (162.4, -70.2)
- added C181: C_100n_0402, antmicro-footprints:0402-cap, F.Cu at (151.9, -60.1)
- added C182: C_100n_0402, antmicro-footprints:0402-cap, F.Cu at (164.8, -73.5)
- added C183: C_100n_0402, antmicro-footprints:0402-cap, F.Cu at (151.9, -62.0)
- added C184: C_100n_0402, antmicro-footprints:0402-cap, F.Cu at (156.6, -65.3)
- added C185: C_100n_0402, antmicro-footprints:0402-cap, F.Cu at (159.5, -68.2)
- added C186: C_100n_0402, antmicro-footprints:0402-cap, F.Cu at (165.8, -75.5)
- added C187: C_100n_0402, antmicro-footprints:0402-cap, F.Cu at (160.6, -62.3)
- added C188: C_100n_0402, antmicro-footprints:0402-cap, F.Cu at (154.8, -62.0)
- added C189: C_100n_0402, antmicro-footprints:0402-cap, F.Cu at (196.6, -58.3)
- added C190: C_100n_0402, antmicro-footprints:0402-cap, F.Cu at (181.2, -42.7)
- added C191: C_100p_0402, antmicro-footprints:0402-cap, F.Cu at (175.6, -37.1)
- added C192: C_100n_0402, antmicro-footprints:0402-cap, F.Cu at (178.5, -39.0)
- added C193: C_100n_0402, antmicro-footprints:0402-cap, F.Cu at (178.5, -37.1)
- added C194: C_1u_0402, antmicro-footprints:0402-cap, F.Cu at (148.1, -24.1)
- added C195: C_100n_0402, antmicro-footprints:0402-cap, F.Cu at (144.8, -16.0)
- added C196: C_100n_0402, antmicro-footprints:0402-cap, F.Cu at (151.0, -24.1)
- added D17: PMEG3010CEJ, antmicro-footprints:SOD-323F, F.Cu at (155.5, -71.8)
- added FB1: BLM15PD121SN1D, antmicro-footprints:0402-res, F.Cu at (159.5, -70.2)
- added FB2: BLM15PD121SN1D, antmicro-footprints:0402-res, F.Cu at (168.7, -75.6)
- added FB3: BLM15PD121SN1D, antmicro-footprints:0402-res, F.Cu at (159.5, -66.3)
- added J7: 0878311420, antmicro-footprints:PinHeader_2x7_P2mm_Drill1mm, F.Cu at (145.1, -80.1)
- added J8: SSW-106-02-G-D-RA, antmicro-footprints:SAMTEC_SSW-106-02-G-D-RA, F.Cu at (128.3, -14.3)
- added L9: PFL1609-102MEW, antmicro-footprints:0603-res, F.Cu at (146.4, -62.6)
- added N2: oshw_logo, antmicro-footprints:oshw-logo, F.Cu at (20.0, -79.5)
- added Q5: BSS138-7-F, antmicro-footprints:SOT-23-3, F.Cu at (151.1, -74.0)
- added Q6: BSS138-7-F, antmicro-footprints:SOT-23-3, F.Cu at (143.0, -66.4)
- added Q7: BSS138-7-F, antmicro-footprints:SOT-23-3, F.Cu at (159.3, -80.5)
- added Q8: BSS138-7-F, antmicro-footprints:SOT-23-3, F.Cu at (-13.9, 3.84)
- added R72: R_100k_0402, antmicro-footprints:0402-res, F.Cu at (146.1, -60.4)
- added R73: R_15k_0603, antmicro-footprints:0603-res, F.Cu at (167.2, -81.8)
- added R74: R_33k2_0402, antmicro-footprints:0402-res, F.Cu at (150.8, -64.0)
- added R75: R_10k_0402, antmicro-footprints:0402-res, F.Cu at (166.9, -79.6)
- added R76: R_10k_0402, antmicro-footprints:0402-res, F.Cu at (131.4, -59.9)
- added R77: R_2k_0402, antmicro-footprints:0402-res, F.Cu at (153.7, -66.0)
- added R78: R_10k_0402, antmicro-footprints:0402-res, F.Cu at (162.9, -75.5)
- added R79: R_10k_0402, antmicro-footprints:0402-res, F.Cu at (149.0, -60.4)
- added R80: R_12k_0402, antmicro-footprints:0402-res, F.Cu at (156.6, -69.3)
- added R81: R_10k_0402, antmicro-footprints:0402-res, F.Cu at (156.6, -67.3)
- added R82: R_10k_0402, antmicro-footprints:0402-res, F.Cu at (161.9, -72.2)
- added R83: R_10k_0402, antmicro-footprints:0402-res, F.Cu at (153.7, -64.0)
- added R84: R_10k_0402, antmicro-footprints:0402-res, F.Cu at (166.6, -77.6)
- added R85: R_10k_0402, antmicro-footprints:0402-res, F.Cu at (150.8, -66.0)
- added R86: R_10k_0402, antmicro-footprints:0402-res, F.Cu at (159.0, -72.2)
- added R87: R_10k_0402, antmicro-footprints:0402-res, F.Cu at (154.9, -75.4)
- added R88: R_100k_0402, antmicro-footprints:0402-res, F.Cu at (-34.3, 15.5)
- added R89: R_100k_0402, antmicro-footprints:0402-res, F.Cu at (-17.9, 14.3)
- added R90: R_100k_0402, antmicro-footprints:0402-res, F.Cu at (-11.3, 7.31)
- added R91: R_100k_0402, antmicro-footprints:0402-res, F.Cu at (-25.5, 16.4)
- added R92: R_100k_0402, antmicro-footprints:0402-res, F.Cu at (-22.6, 16.2)
- added R93: R_10k_0402, antmicro-footprints:0402-res, F.Cu at (-17.9, 12.3)
- added R94: R_200k_0402, antmicro-footprints:0402-res, F.Cu at (181.4, -36.7)
- added R95: R_2k2_0402, antmicro-footprints:0402-res, F.Cu at (175.6, -39.0)
- added R96: R_2k2_0402, antmicro-footprints:0402-res, F.Cu at (181.4, -38.7)
- added R97: R_1k_0402, antmicro-footprints:0402-res, F.Cu at (181.4, -40.7)
- added U34: AP62301WU-7, antmicro-footprints:TSOT23-6, F.Cu at (138.3, -62.8)
- added U35: 93LC56CT-IMC, antmicro-footprints:DFN-8_2x3mm, F.Cu at (159.2, -75.6)
- added U36: SN74AVC2T245RSWR, antmicro-footprints:Texas_RSW0010A, F.Cu at (142.8, -61.9)
- added U37: SN74AVC2T245RSWR, antmicro-footprints:Texas_RSW0010A, F.Cu at (147.5, -66.8)
- added U38: SN74AVC4T245PWR, Package_SO:TSSOP-16_4.4x5mm_P0.65mm, F.Cu at (144.4, -72.1)
- added U39: SN74AVC4T245PWR, Package_SO:TSSOP-16_4.4x5mm_P0.65mm, F.Cu at (152.5, -79.7)
- added U40: NC7WZ07P6X, antmicro-footprints:SOT-363, F.Cu at (163.5, -81.0)
- added U41: PCA9306D_118, antmicro-footprints:SOIC-8_W3.9mm, F.Cu at (170.9, -39.5)
- added U42: M24C64-FMC6TG, antmicro-footprints:STM_UFDFPN8DFN8_2X3, F.Cu at (177.2, -41.9)
- added U43: TPD4E05U06QDQARQ1, antmicro-footprints:TPD4E05U06QDQARQ1, F.Cu at (145.1, -19.0)
- added U44: TPD4E05U06QDQARQ1, antmicro-footprints:TPD4E05U06QDQARQ1, F.Cu at (145.1, -23.1)
- added Y2: ABM8G-12.000MHZ-18-D2Y-T, antmicro-footprints:KX-7, F.Cu at (133.3, -63.2)
- moved C152 223.1 mm to (-28.4, 16.4)
- moved R70 220.8 mm to (-37.2, 15.5)
- moved C153 214.3 mm to (-23.7, 12.3)
- moved U31 213.9 mm to (-27.5, 12.7)
- moved U29 213.9 mm to (-33.7, 10.5)
- moved C154 213.0 mm to (-17.2, 7.31)
- moved R68 211.5 mm to (-15.0, 11.3)
- moved R71 210.8 mm to (-17.2, 9.30)
- moved C156 209.8 mm to (-23.7, 14.3)
- moved C151 209.1 mm to (-31.3, 15.5)
- moved S1 206.5 mm to (-19.8, 3.69)
- moved C149 204.6 mm to (-11.3, 9.30)
- moved U30 204.1 mm to (-34.2, 4.66)
- moved R67 203.8 mm to (-14.3, 9.30)
- moved C155 201.4 mm to (-20.8, 12.3)
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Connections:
- net /Debug/PD_CC1 renamed /Debug and JTAG/PD_CC1
- net /Debug/PD_CC2 renamed /Debug and JTAG/PD_CC2
- net Net-(U29-Pad14) renamed /Reset logic/PS_RST
- net Net-(U30-Pad14) renamed /Reset logic/PL_RST
- D8 pad 1: /Power Supply/USB-C socket/DBG_USB_P -> /Debug and JTAG/DBG_USB_N
- D8 pad 2: /Power Supply/USB-C socket/DBG_USB_N -> /Debug and JTAG/DBG_USB_P
- J2 pad A6: /Power Supply/USB-C socket/DBG_USB_P -> /Debug and JTAG/DBG_USB_P
- J2 pad A7: /Power Supply/USB-C socket/DBG_USB_N -> /Debug and JTAG/DBG_USB_N
- J2 pad B6: /Power Supply/USB-C socket/DBG_USB_P -> /Debug and JTAG/DBG_USB_P
- J2 pad B7: /Power Supply/USB-C socket/DBG_USB_N -> /Debug and JTAG/DBG_USB_N
- J_SOM240_1 pad A17: /Xilinx K26 SOM/HDA11 -> /PMOD/HDA11
- J_SOM240_1 pad A22: /Xilinx K26 SOM/JTAG_TMS_C2M -> /Debug and JTAG/JTAG_TMS_C2M
- J_SOM240_1 pad A23: /Xilinx K26 SOM/JTAG_TDO_M2C -> /Debug and JTAG/JTAG_TDO_M2C
- J_SOM240_1 pad A24: /Xilinx K26 SOM/JTAG_TDI_C2M -> /Debug and JTAG/JTAG_TDI_C2M
- J_SOM240_1 pad A25: /Xilinx K26 SOM/JTAG_TCK_C2M -> /Debug and JTAG/JTAG_TCK_C2M
- J_SOM240_1 pad B20: /Xilinx K26 SOM/HDA15 -> /PMOD/HDA15
- J_SOM240_1 pad B21: /Xilinx K26 SOM/HDA16_CC -> /PMOD/HDA16_CC
- J_SOM240_1 pad B22: /Xilinx K26 SOM/HDA17 -> /PMOD/HDA17
- J_SOM240_1 pad B29: /Xilinx K26 SOM/MIO36 -> /Debug and JTAG/MIO36
- J_SOM240_1 pad B30: /Xilinx K26 SOM/MIO37 -> /Debug and JTAG/MIO37
- J_SOM240_1 pad C15: /Xilinx K26 SOM/PS_POR_L -> /Debug and JTAG/~PS_POR
- J_SOM240_1 pad C22: /Xilinx K26 SOM/HDA18 -> /PMOD/HDA18
- J_SOM240_1 pad C26: /Xilinx K26 SOM/MIO24_I2C_SCK -> /I2C /MIO24_I2C_SCK
- J_SOM240_1 pad C27: /Xilinx K26 SOM/MIO25_I2C_SDA -> /I2C /MIO24_I2C_SDA
- J_SOM240_1 pad D20: /Xilinx K26 SOM/HDA12 -> /PMOD/HDA12
- J_SOM240_1 pad D21: /Xilinx K26 SOM/HDA13 -> /PMOD/HDA13
- J_SOM240_1 pad D22: /Xilinx K26 SOM/HDA14 -> /PMOD/HDA14
- U23 pad 10: Net-(U23-Pad10) -> /Debug and JTAG/USB_3V45
- U23 pad 11: Net-(U23-Pad11) -> /Debug and JTAG/FTDI_TDO
- U23 pad 12: Net-(U23-Pad12) -> /Debug and JTAG/FTDI_TMS
- U23 pad 13: Net-(U23-Pad13) -> /Debug and JTAG/JTAG_VCCO_ON
- U23 pad 14: Net-(U23-Pad14) -> /Debug and JTAG/~FTDI_LS_OE
- U23 pad 15: Net-(U23-Pad15) -> /Debug and JTAG/~FTDI_PS_POR
- U23 pad 16: Net-(U23-Pad16) -> /Debug and JTAG/~FTDI_PS_SRST
- U23 pad 17: Net-(U23-Pad17) -> /Debug and JTAG/FTDI_UARTB_TXD
- U23 pad 18: Net-(U23-Pad18) -> /Debug and JTAG/FTDI_UARTB_RXD
- U23 pad 25: Net-(U23-Pad25) -> /Debug and JTAG/USB_1V2
- U23 pad 26: Net-(U23-Pad26) -> /Debug and JTAG/USB_3V45
- U23 pad 27: Net-(U23-Pad27) -> /Debug and JTAG/XIN
- U23 pad 28: Net-(U23-Pad28) -> /Debug and JTAG/XOUT
- U23 pad 29: Net-(U23-Pad29) -> GND
- U23 pad 3: Net-(U23-Pad3) -> GND
- U23 pad 30: Net-(U23-Pad30) -> /Debug and JTAG/VREGIN
- U23 pad 31: Net-(U23-Pad31) -> /Debug and JTAG/USB_1V2
- U23 pad 39: Net-(U23-Pad39) -> /Debug and JTAG/USB_3V45
- U23 pad 44: Net-(U23-Pad44) -> /Debug and JTAG/USB_1V2
- U23 pad 46: Net-(U23-Pad46) -> /Debug and JTAG/FTDI_EEPROM_WC
- U23 pad 5: (no net) -> Net-(U23-Pad5)
- U23 pad 54: (no net) -> Net-(U23-Pad54)
- U23 pad 55: (no net) -> Net-(U23-Pad55)
- U23 pad 56: (no net) -> Net-(U23-Pad56)
- U23 pad 57: Net-(U23-Pad57) -> /Debug and JTAG/VCC_USB
- U23 pad 58: Net-(U23-Pad58) -> /Debug and JTAG/DBG_USB_N
- U23 pad 59: Net-(U23-Pad59) -> /Debug and JTAG/DBG_USB_P
- U23 pad 6: Net-(U23-Pad6) -> /Debug and JTAG/FTDI_TCK
- U23 pad 61: Net-(U23-Pad61) -> /Debug and JTAG/VCC_PD
- U23 pad 63: Net-(U23-Pad63) -> /Debug and JTAG/PD1_SVBUS
- U23 pad 66: Net-(U23-Pad66) -> /Debug and JTAG/USB_1V2
- U23 pad 67: Net-(U23-Pad67) -> /Debug and JTAG/~FTDI_PWREN
- U23 pad 69: Net-(U23-Pad69) -> GND
- U23 pad 7: Net-(U23-Pad7) -> /Debug and JTAG/FTDI_TDI
- U23 pad 8: Net-(U23-Pad8) -> /Debug and JTAG/USB_1V2
- U23 pad 9: Net-(U23-Pad9) -> GND
